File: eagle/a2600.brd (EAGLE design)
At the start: 108.9 x 85.8 mm, 87 parts, among them IC1 74LS245N, IC2 74LS245N, IC3 74LS245N, IC5 7805TV, T1 2N3906, T2 2N3904, T3 2N3906, T4 2N3904, X1 FMS6141

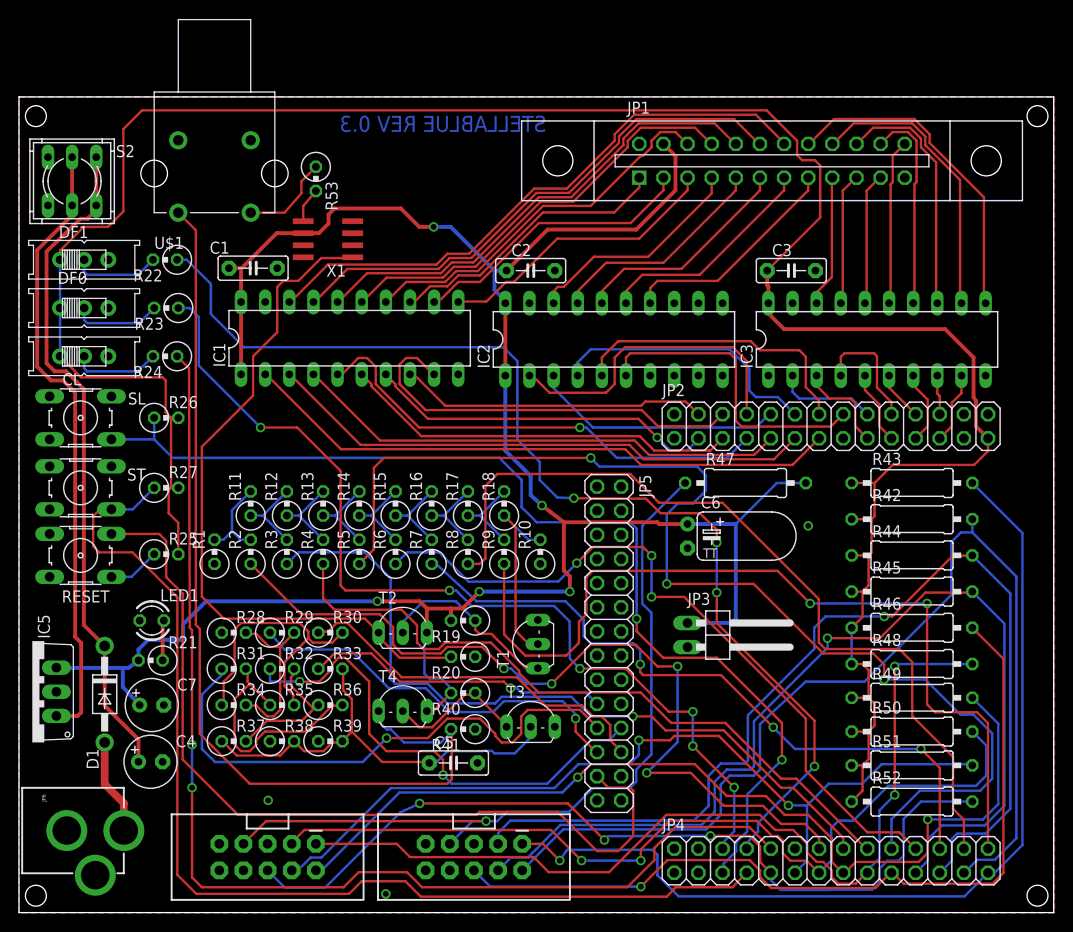
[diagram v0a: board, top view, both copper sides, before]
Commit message: PCB layout manual enhancements. Still in progress
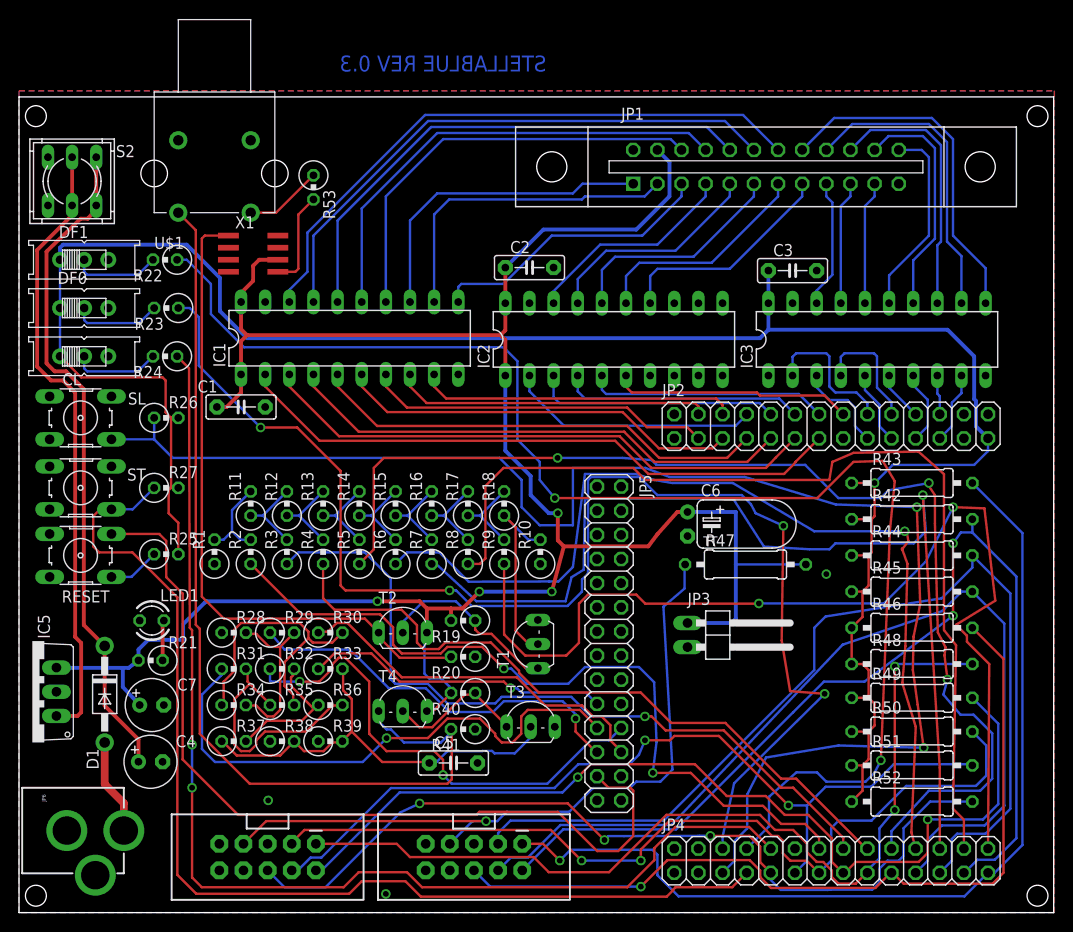
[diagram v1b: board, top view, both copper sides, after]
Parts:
- moved C1 14.7 mm to (22.9, 52.5)
- moved R47 8.57 mm to (75.9, 35.9)
- moved X1 8.02 mm to (24.1, 68.6), turned to 270 degrees
- moved C6 1.27 mm to (69.8, 40.1)
- moved R53 0.92 mm to (30.5, 75.6)
- moved JP1 0.90 mm to (78.1, 77.7)
- moved C2 0.34 mm to (53.2, 67.1)
- moved C3 0.13 mm to (80.9, 66.8)
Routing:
- net SL: track 111.6 -> 154.9 mm
- net DF0: track 100.8 -> 142.4 mm, vias 6 -> 4
- net CV5: track 73.2 -> 107.7 mm, vias 3 -> 1
- net DF1: track 117.1 -> 146.8 mm, vias 4 -> 2
- net +3V3: track 252.9 -> 227.6 mm, vias 0 -> 1
- net CV4: track 76.9 -> 100.5 mm, vias 3 -> 1
- net CV7: track 92.6 -> 109.4 mm
- net CV6: track 87.9 -> 102.3 mm
- net N$29: track 43.0 -> 33.4 mm
- net J+5V: track 83.2 -> 75.8 mm
- net CV0: track 89.1 -> 81.8 mm, vias 4 -> 2
- net N$34: track 32.5 -> 25.2 mm
- net N$30: track 33.5 -> 26.5 mm
- net VIDEO: track 3.66 -> 10.3 mm
- net N$33: track 31.4 -> 25.4 mm
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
